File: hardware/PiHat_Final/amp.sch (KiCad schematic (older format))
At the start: 1 part, among them J2 RPi_GPIO

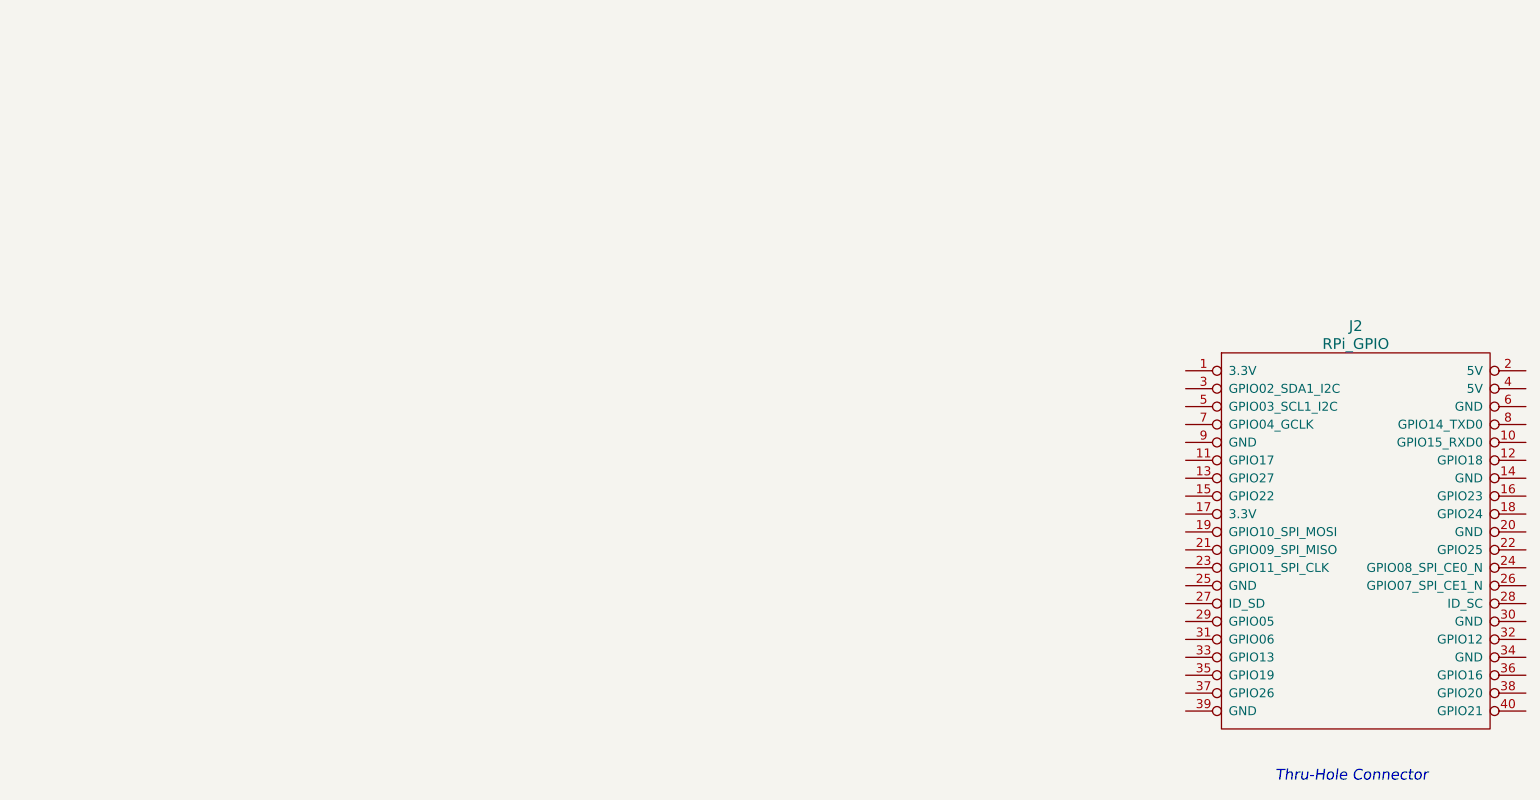
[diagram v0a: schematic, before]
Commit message: Began work on RX/TX schematic.
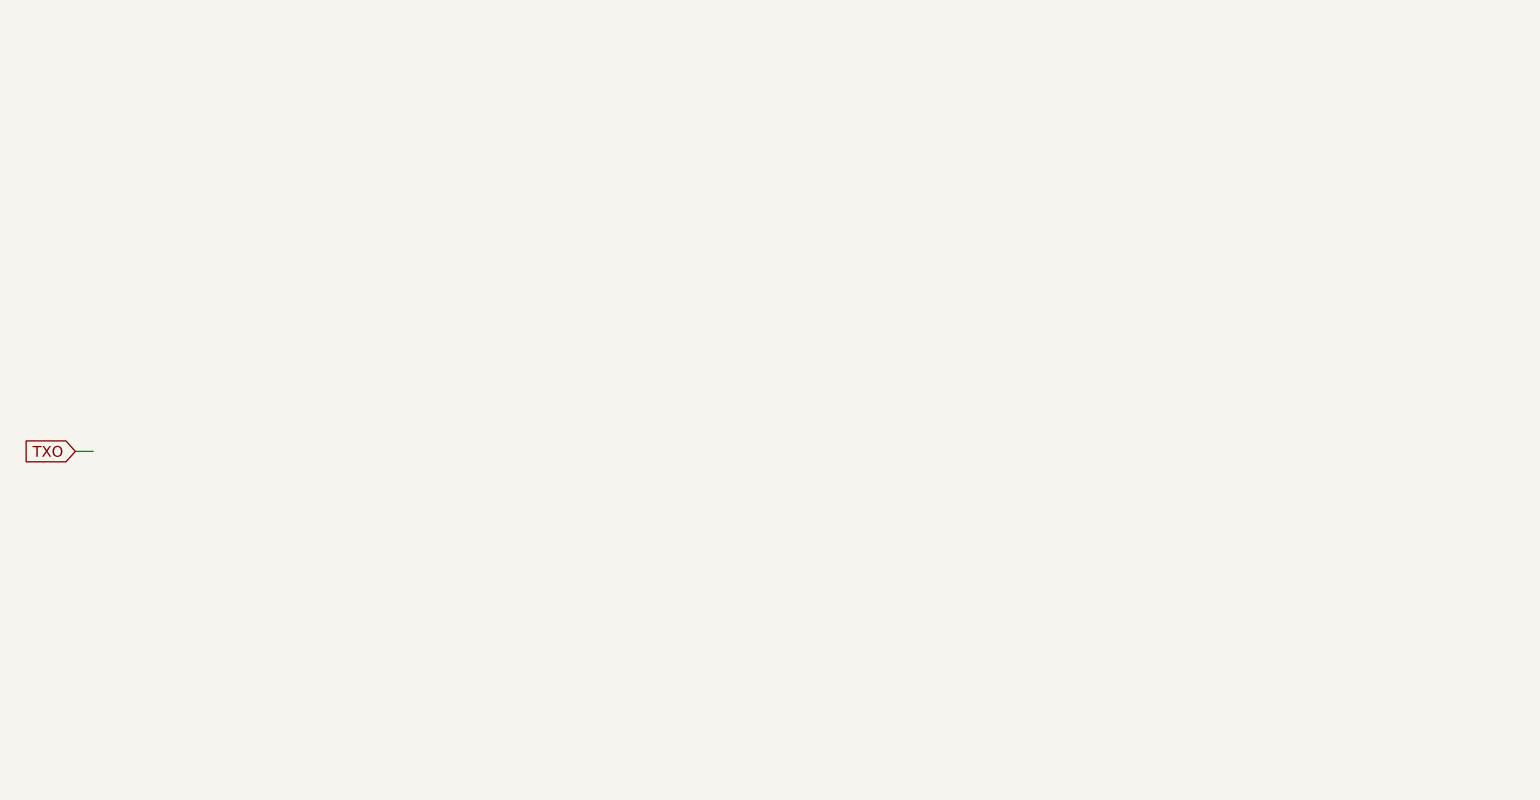
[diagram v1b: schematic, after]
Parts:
- removed J2: RPi_GPIO, RPi_Hat:Pin_Header_Straight_2x20, symbol RPi_GPIO
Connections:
- net labels added: TXO
- wire segments 0 -> 1
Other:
- note removed: "Thru-Hole Connector"
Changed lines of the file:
@@
 $Descr A4 11693 8268
 encoding utf-8
-Sheet 2 6
+Sheet 5 6
 Title ""
 Date ""
@@
 Comment4 ""
 $EndDescr
-$Comp
-L RPi_GPIO J2
-U 1 1 5516AE26
-P 7500 2700
-F 0 "J2" H 8250 2950 60  0000 C CNN
-F 1 "RPi_GPIO" H 8250 2850 60  0000 C CNN
-F 2 "RPi_Hat:Pin_Header_Straight_2x20" H 7500 2700 60  0001 C CNN
-F 3 "" H 7500 2700 60  0000 C CNN
-	1    7500 2700
-	1    0    0    -1
-$EndComp
-Text Notes 7800 5000 0    60   Italic 0
-Thru-Hole Connector
+Text GLabel 1100 3150 0    60   Input ~ 0
+TXO
+Wire Wire Line
+	1100 3150 1200 3150
 $EndSCHEMATC

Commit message: Added more to the Schematic.
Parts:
- added C16, C17, C18, C19, C20, C21, C22, C23, C24, C25, C26, C27, C28, C29, C30, C31: C, Capacitors_SMD:C_0805, symbol C
- added L10, L11, L12, L13, L14, L6, L7, L8, L9: L_Small, Resistors_SMD:R_0603, symbol L_Small
- added Q1: AFT05MS003N, TO_SOT_Packages_SMD:SOT89-3_Housing_Handsoldering, symbol Q_NMOS_GSD
- added R7, R8, R9: R, Resistors_SMD:R_0603_HandSoldering, symbol R
- added RV1: POT, RFBRD:J-FOOT_POT, symbol POT
- added U5: MMG3H21NT1, TO_SOT_Packages_SMD:SOT89-3_Housing_Handsoldering, symbol MMG3H21NT1
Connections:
- net labels added: +5V, GND, TX_PWR
- wire segments 1 -> 59

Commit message: Began Layout, Pihat final.
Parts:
- RV1: footprint RFBRD:J-FOOT_POT -> Potentiometers:Potentiometer_Bourns_3006W_Angular_ScrewFront
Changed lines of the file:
@@
 LIBS:contrib
 LIBS:valves
-LIBS:RFT
 LIBS:RPi_Hat-cache
 EELAYER 25 0
@@
 	1900 3600 1900 3700
 $Comp
-L GND #PWR30
+L GND #PWR030
 U 1 1 58EEB422
 P 1900 3700
-F 0 "#PWR30" H 1900 3450 50  0001 C CNN
+F 0 "#PWR030" H 1900 3450 50  0001 C CNN
 F 1 "GND" H 1900 3550 50  0000 C CNN
 F 2 "" H 1900 3700 50  0000 C CNN
@@
 Connection ~ 3000 2750
 $Comp
-L GND #PWR32
+L GND #PWR031
 U 1 1 58EEB55A
 P 3000 2850
-F 0 "#PWR32" H 3000 2600 50  0001 C CNN
+F 0 "#PWR031" H 3000 2600 50  0001 C CNN
 F 1 "GND" H 3000 2700 50  0000 C CNN
 F 2 "" H 3000 2850 50  0000 C CNN
@@
 Connection ~ 2500 2450
 $Comp
-L +5V #PWR31
+L +5V #PWR032
 U 1 1 58EEB63A
 P 2500 2350
-F 0 "#PWR31" H 2500 2200 50  0001 C CNN
+F 0 "#PWR032" H 2500 2200 50  0001 C CNN
 F 1 "+5V" H 2500 2490 50  0000 C CNN
 F 2 "" H 2500 2350 50  0000 C CNN
@@
 	4050 3550 4050 3650
 $Comp
-L GND #PWR37
+L GND #PWR033
 U 1 1 58EEBCF1
 P 4050 3650
-F 0 "#PWR37" H 4050 3400 50  0001 C CNN
+F 0 "#PWR033" H 4050 3400 50  0001 C CNN
 F 1 "GND" H 4050 3500 50  0000 C CNN
 F 2 "" H 4050 3650 50  0000 C CNN
@@
 $EndComp
 $Comp
-L GND #PWR34
+L GND #PWR034
 U 1 1 58EEBD27
 P 3650 3650
-F 0 "#PWR34" H 3650 3400 50  0001 C CNN
+F 0 "#PWR034" H 3650 3400 50  0001 C CNN
 F 1 "GND" H 3650 3500 50  0000 C CNN
 F 2 "" H 3650 3650 50  0000 C CNN
@@
 	3850 2350 3850 2450
 $Comp
-L GND #PWR36
+L GND #PWR035
 U 1 1 58EECAA9
 P 3850 2450
-F 0 "#PWR36" H 3850 2200 50  0001 C CNN
+F 0 "#PWR035" H 3850 2200 50  0001 C CNN
 F 1 "GND" H 3850 2300 50  0000 C CNN
 F 2 "" H 3850 2450 50  0000 C CNN
@@
 F 0 "RV1" H 4100 1270 50  0000 C CNN
 F 1 "POT" H 4100 1350 50  0000 C CNN
-F 2 "RFBRD:J-FOOT_POT" H 4100 1350 50  0001 C CNN
+F 2 "Potentiometers:Potentiometer_Bourns_3006W_Angular_ScrewFront" H 4100 1350 50  0001 C CNN
 F 3 "" H 4100 1350 50  0000 C CNN
 	1    4100 1350
@@
 	4100 1500 4100 1600
 $Comp
-L GND #PWR39
+L GND #PWR036
 U 1 1 58EECFD7
 P 4100 1600
-F 0 "#PWR39" H 4100 1350 50  0001 C CNN
+F 0 "#PWR036" H 4100 1350 50  0001 C CNN
 F 1 "GND" H 4200 1600 50  0000 C CNN
 F 2 "" H 4100 1600 50  0000 C CNN
@@
 	4100 900  4100 1200
 $Comp
-L +5V #PWR38
+L +5V #PWR037
 U 1 1 58EED25C
 P 4100 900
-F 0 "#PWR38" H 4100 750 50  0001 C CNN
+F 0 "#PWR037" H 4100 750 50  0001 C CNN
 F 1 "+5V" H 4100 1040 50  0000 C CNN
 F 2 "" H 4100 900 50  0000 C CNN
@@
 	3600 1100 3600 1200
 $Comp
-L GND #PWR33
+L GND #PWR038
 U 1 1 58EED35D
 P 3600 1200
-F 0 "#PWR33" H 3600 950 50  0001 C CNN
+F 0 "#PWR038" H 3600 950 50  0001 C CNN
 F 1 "GND" H 3600 1050 50  0000 C CNN
 F 2 "" H 3600 1200 50  0000 C CNN
@@
 $EndComp
 $Comp
-L GND #PWR35
+L GND #PWR039
 U 1 1 58EED3AB
 P 3850 1950
-F 0 "#PWR35" H 3850 1700 50  0001 C CNN
+F 0 "#PWR039" H 3850 1700 50  0001 C CNN
 F 1 "GND" H 3850 1800 50  0000 C CNN
 F 2 "" H 3850 1950 50  0000 C CNN
@@
 	5350 3350 5350 3450
 $Comp
-L GND #PWR41
+L GND #PWR040
 U 1 1 58EED9F7
 P 5350 3450
-F 0 "#PWR41" H 5350 3200 50  0001 C CNN
+F 0 "#PWR040" H 5350 3200 50  0001 C CNN
 F 1 "GND" H 5350 3300 50  0000 C CNN
 F 2 "" H 5350 3450 50  0000 C CNN
@@
 Connection ~ 4850 1800
 $Comp
-L GND #PWR40
+L GND #PWR041
 U 1 1 58EEE441
 P 4850 1900
-F 0 "#PWR40" H 4850 1650 50  0001 C CNN
+F 0 "#PWR041" H 4850 1650 50  0001 C CNN
 F 1 "GND" H 4850 1750 50  0000 C CNN
 F 2 "" H 4850 1900 50  0000 C CNN
@@
 	6050 3250 6050 3350
 $Comp
-L GND #PWR42
+L GND #PWR042
 U 1 1 58EEF4E6
 P 6050 3350
-F 0 "#PWR42" H 6050 3100 50  0001 C CNN
+F 0 "#PWR042" H 6050 3100 50  0001 C CNN
 F 1 "GND" H 6050 3200 50  0000 C CNN
 F 2 "" H 6050 3350 50  0000 C CNN
@@
 $EndComp
 $Comp
-L GND #PWR43
+L GND #PWR043
 U 1 1 58EEF555
 P 6450 3350
-F 0 "#PWR43" H 6450 3100 50  0001 C CNN
+F 0 "#PWR043" H 6450 3100 50  0001 C CNN
 F 1 "GND" H 6450 3200 50  0000 C CNN
 F 2 "" H 6450 3350 50  0000 C CNN
@@
 $EndComp
 $Comp
-L GND #PWR44
+L GND #PWR044
 U 1 1 58EEF5BD
 P 6850 3350
-F 0 "#PWR44" H 6850 3100 50  0001 C CNN
+F 0 "#PWR044" H 6850 3100 50  0001 C CNN
 F 1 "GND" H 6850 3200 50  0000 C CNN
 F 2 "" H 6850 3350 50  0000 C CNN

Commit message: PCB Layout Changes
minor changes, will continue layout
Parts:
- RV1: symbol POT -> POT-RESCUE-RPi_Hat
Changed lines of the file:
@@
 EESchema Schematic File Version 2
+LIBS:RPi_Hat-rescue
 LIBS:power
 LIBS:device
@@
 	4350 1350 4350 1550
 $Comp
-L POT RV1
+L POT-RESCUE-RPi_Hat RV1
 U 1 1 58EECEFA
 P 4100 1350
